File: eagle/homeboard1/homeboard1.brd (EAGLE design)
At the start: 100 x 80 mm, 17 parts, among them U1 XC3S400TQ144

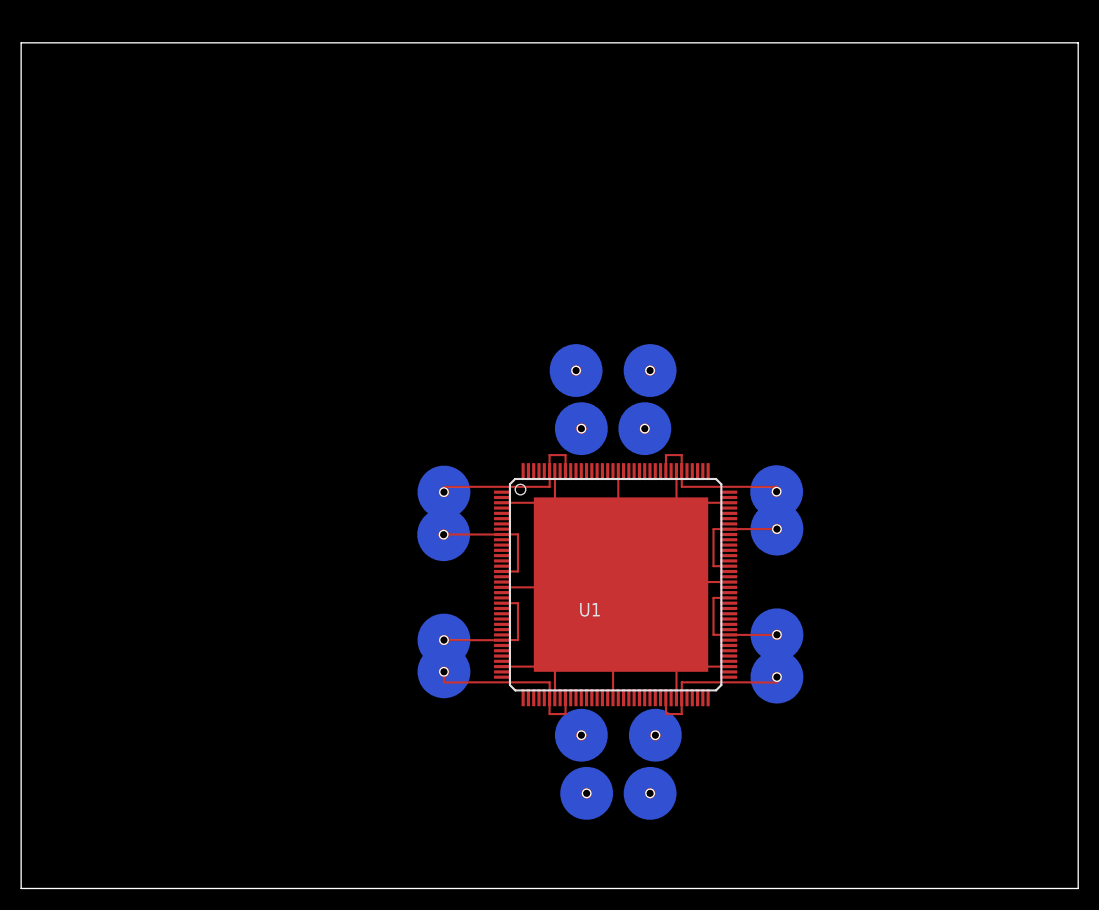
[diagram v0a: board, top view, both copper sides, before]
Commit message: added ram chip
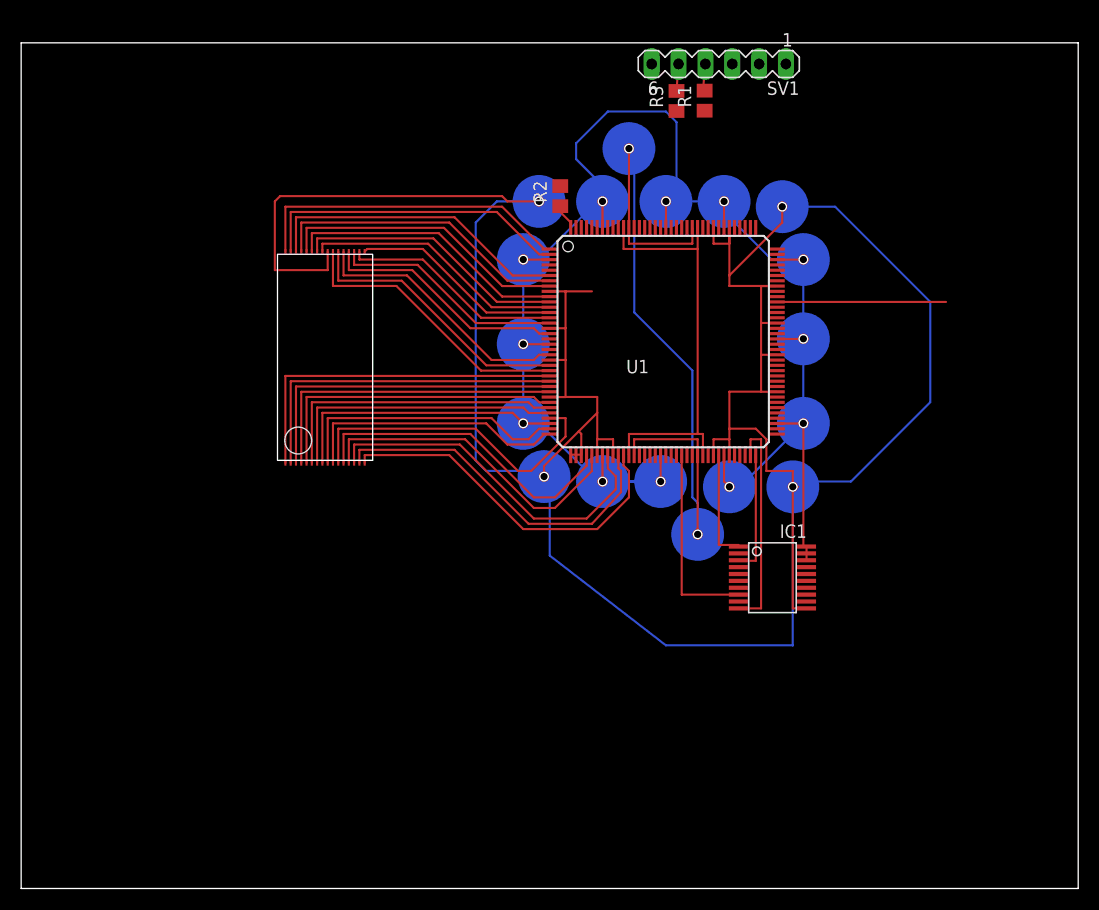
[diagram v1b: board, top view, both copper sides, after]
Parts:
- removed U$12, U$13, U$16, U$17, U$21, U$22, U$24, U$8, U$9: VIA_DIY, cpcfpga:VIA_DIY
- added IC1: XCF02S, smd-special:VO20
- added R1, R2, R3: 100, rcl:R0805
- added SV1: (no value), con-lstb:MA06-1
- added U$10, U$14, U$15, U$18, U$19, U$25, U$26, U$27, U$28, U$29, U$6, U$7: VIA_DIY, cpcfpga:VIA_DIY
- U$4: value VIA_DIY -> AS6C4008; device cpcfpga:VIA_DIY -> cpcfpga:TSOP32
- moved U$23 61.0 mm to (57.5, 70.0)
- moved U$3 51.7 mm to (49.0, 65.0)
- moved U$20 41.9 mm to (72.0, 64.5)
- moved U$4 30.8 mm to (28.8, 50.0), turned to 90 degrees
- moved U$1 26.7 mm to (64.0, 33.5)
- moved U1 23.4 mm to (60.7, 51.7)
- moved U$2 15.0 mm to (73.0, 38.0)
- moved U$5 11.0 mm to (49.5, 39.0)
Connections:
- removed net GND_B: U$12.B, U$13.B, U$16.B, U$17.B, U$20.B, U$5.B, U$8.B, U$9.B
- removed net VCCINT01: U$1.T, U1.P49
- new net N$10: U$4.P29, U1.P7
- new net N$11: U$4.P28, U1.P8
- new net N$14: U$14.T, U1.P34
- new net N$15: U$15.T, U1.P19
- new net N$22: U$4.P27, U1.P10
- new net N$23: U$4.P26, U1.P11
- new net N$24: U$4.P18, U1.P14
- new net N$25: U$25.T, U1.P54
- new net N$26: IC1.18, IC1.19, IC1.20, U$29.T, U1.P75
- new net N$27: U$4.P19, U1.P15
- new net N$28: U$28.T, U1.P91
- new net N$29: U$4.P20, U1.P17
- new net N$3: U$10.T, U1.P126
- new net N$30: U$4.P21, U1.P21
- new net N$31: U$4.P22, U1.P23
- new net N$32: U$4.P23, U1.P24
- new net N$33: U$4.P1, U1.P25
- new net N$34: U$4.P2, U1.P26
- new net N$35: U$4.P3, U1.P27
- new net N$36: U$4.P4, U1.P28
- new net N$37: U$4.P5, U1.P30
- new net N$38: U$4.P6, U1.P31
- new net N$39: U$4.P7, U1.P32
- new net N$40: U$4.P11, U1.P33
- new net N$41: U$4.P9, U1.P35
- new net N$42: U$4.P10, U1.P36
- new net N$43: U$4.P12, U1.P40
- new net N$44: U$4.P13, U1.P41
- new net N$45: U$4.P14, U1.P44
- new net N$46: U$4.P15, U1.P46
- new net N$47: U$4.P16, U1.P47
- new net N$5: U$4.P25, U1.P12
- new net N$6: U$4.P17, U1.P13
- new net N$7: U$4.P30, U1.P6
- new net TCK: IC1.6, R1.2, SV1.4
- new net TDI: IC1.4, SV1.3
- new net TDO: SV1.6, U1.P109
- new net TMS: IC1.5, R3.2, SV1.5
- net GND: now also IC1.11, U$2.B, U$20.B, U$3.B, U$3.T, U$4.P24, U$5.B, U$5.T, U1.P16, U1.P22, U1.P29, U1.P37, U1.P38, U1.P39, U1.P42, U1.P45, U1.P9; no longer U$20.T
- net N$1: now also U$4.P32, U1.P1; no longer U$5.T, U1.P16, U1.P9
- net N$12: now also R2.1, U1.P144; no longer U$16.T, U1.P101, U1.P94
- net N$13: now also IC1.17, R2.2; no longer U$17.T, U1.P114, U1.P117
- net N$16: now also R3.1, U1.P111; no longer U$22.T, U1.P48
- net N$17: now also IC1.7, U1.P143; no longer U$24.T, U1.P133
- net N$18: now also IC1.8, U1.P58; no longer U$23.T, U1.P61
- net N$19: now also IC1.3, U1.P72; no longer U$21.T, U1.P134
- net N$2: now also U$4.P31, U1.P2; no longer U$9.T, U1.P42, U1.P45
- net N$20: now also IC1.10, U1.P71; no longer U$21.B, U$22.B, U$3.B, U$4.B
- net N$21: now also U1.P98; no longer U$3.T, U1.P62
- net N$4: now also U$2.T, U$20.T, U1.P101, U1.P114, U1.P117, U1.P64, U1.P67, U1.P81, U1.P88, U1.P94; no longer U$8.T, U1.P22, U1.P29
- net N$8: now also R1.1, U1.P110; no longer U$12.T, U1.P64, U1.P67
- net N$9: now also IC1.1, U1.P65; no longer U$13.T, U1.P81, U1.P88
- net VCC: now also U$10.B, U$14.B, U$15.B, U$18.B, U$18.T, U$19.B, U$19.T, U$25.B, U$26.B, U$26.T, U$27.B, U$27.T, U$28.B, U$29.B, U$4.P8, U$6.B, U$6.T, U$7.B, U$7.T; no longer U1.P126, U1.P19, U1.P34, U1.P54, U1.P75, U1.P91
- net VCCAUX: now also U1.P134, U1.P48, U1.P62; no longer U$4.T
- net VCCINT23: now also U$23.T, U1.P133; no longer U$2.T
- net VCCINT_B: now also U$1.T, U1.P49, U1.P61; no longer U$2.B, U$24.B
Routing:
- net GND: track 16.6 -> 222.8 mm
- net VCCINT_B: track 0.00 -> 56.0 mm
- net N$4: track 12.0 -> 61.6 mm
- net VCCAUX: track 0.00 -> 39.4 mm
- net N$47: track 0.00 -> 34.1 mm
- net N$45: track 0.00 -> 34.1 mm
- net N$46: track 0.00 -> 33.8 mm
- net N$33: track 0.00 -> 33.3 mm
- net N$34: track 0.00 -> 32.3 mm
- net N$35: track 0.00 -> 31.3 mm
- net N$40: track 0.00 -> 31.0 mm
- net N$44: track 0.00 -> 30.9 mm
- net N$43: track 0.00 -> 30.5 mm
- net N$36: track 0.00 -> 30.3 mm
- net N$7: track 0.00 -> 29.6 mm
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
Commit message: improved ram chip layout
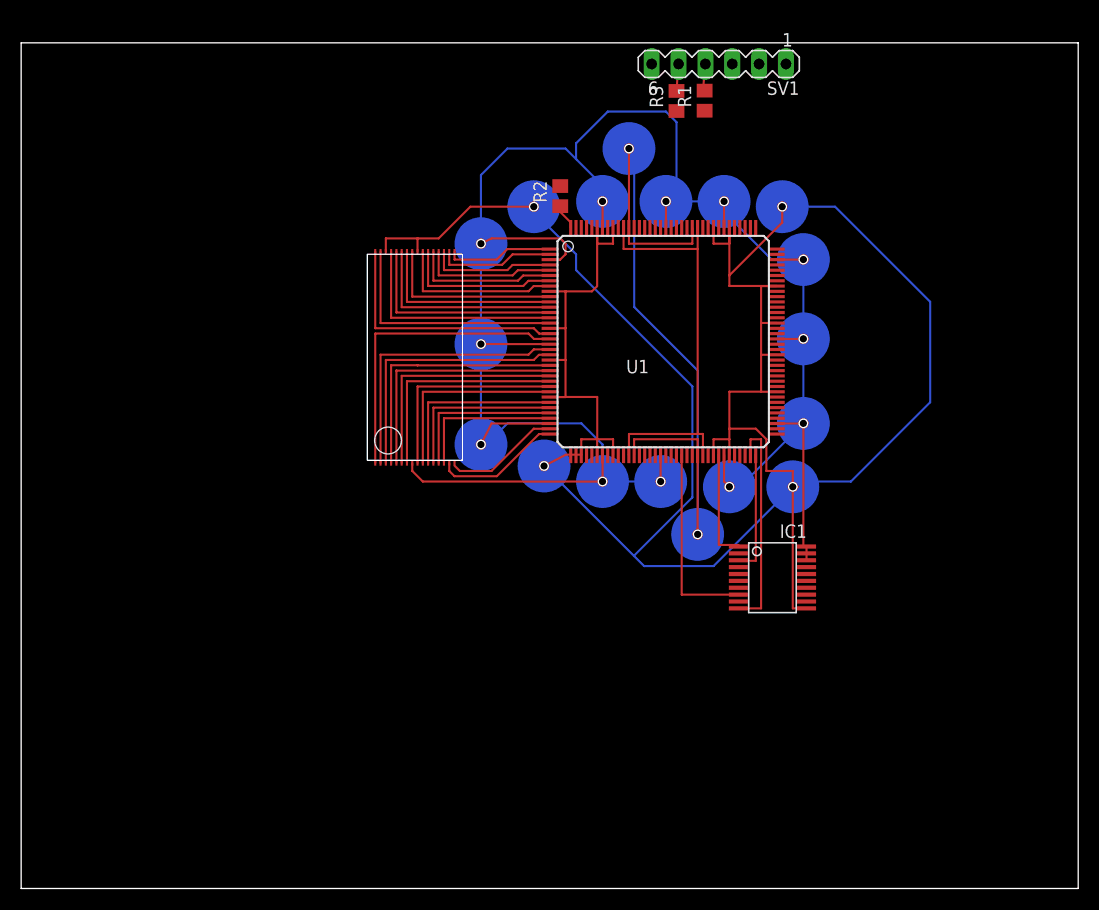
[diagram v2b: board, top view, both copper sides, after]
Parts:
- moved U$4 8.50 mm to (37.2, 50.0)
- moved U$14 4.47 mm to (43.5, 42.0)
- moved U$18 4.27 mm to (43.5, 61.0)
- moved U$15 4.00 mm to (43.5, 51.5)
- moved U$5 1.00 mm to (49.5, 40.0)
- moved U$3 0.71 mm to (48.5, 64.5)
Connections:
- removed net N$39: U$4.P7, U1.P32
- removed net N$40: U$4.P11, U1.P33
- removed net N$41: U$4.P9, U1.P35
- removed net N$42: U$4.P10, U1.P36
- new net N$48: U$4.P20, U1.P5
- new net N$49: U$4.P19, U1.P4
- new net N$50: U$4.P1, U1.P18
- new net N$52: U$4.P4, U1.P23
- new net N$53: U$4.P3, U1.P21
- new net N$54: U$4.P5, U1.P24
- new net N$55: U$4.P6, U1.P25
- new net N$56: U$4.P7, U1.P26
- net GND: now also U$4.P30
- net N$1: now also U$4.P17; no longer U$4.P32
- net N$10: now also U$4.P22; no longer U$4.P29
- net N$11: now also U$4.P23; no longer U$4.P28
- net N$2: now also U$4.P18; no longer U$4.P31
- net N$22: now also U$4.P25; no longer U$4.P27
- net N$24: now also U$4.P29; no longer U$4.P18
- net N$27: now also U$4.P31; no longer U$4.P19
- net N$29: now also U$4.P32; no longer U$4.P20
- net N$30: now also U$4.P10, U1.P28; no longer U$4.P21, U1.P21
- net N$31: now also U$4.P11, U1.P30; no longer U$4.P22, U1.P23
- net N$32: now also U$4.P12, U1.P31; no longer U$4.P23, U1.P24
- net N$33: now also U$4.P2, U1.P20; no longer U$4.P1, U1.P25
- net N$34: now also U$4.P13, U1.P32; no longer U$4.P2, U1.P26
- net N$35: now also U$4.P14, U1.P33; no longer U$4.P3, U1.P27
- net N$36: now also U$4.P9, U1.P27; no longer U$4.P4, U1.P28
- net N$37: now also U$4.P16, U1.P35; no longer U$4.P5, U1.P30
- net N$38: now also U$4.P15, U1.P36; no longer U$4.P6, U1.P31
- net N$43: no longer U$4.P12
- net N$44: no longer U$4.P13
- net N$45: no longer U$4.P14
- net N$46: no longer U$4.P15
- net N$47: no longer U$4.P16
- net N$5: now also U$4.P27; no longer U$4.P25
- net N$6: now also U$4.P28; no longer U$4.P17
- net N$7: now also U$4.P21; no longer U$4.P30
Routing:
- net N$47: track 34.1 -> 0.00 mm
- net N$45: track 34.1 -> 0.00 mm
- net N$46: track 33.8 -> 0.00 mm
- net N$40: track 31.0 -> 0.00 mm
- net N$44: track 30.9 -> 0.00 mm
- net N$43: track 30.5 -> 0.00 mm
- net GND: track 222.8 -> 193.7 mm
- net N$50: track 0.00 -> 29.0 mm
- net N$39: track 27.5 -> 0.00 mm
- net N$41: track 26.5 -> 0.00 mm
- net N$42: track 25.5 -> 0.00 mm
- net N$53: track 0.00 -> 25.5 mm
- net N$52: track 0.00 -> 24.3 mm
- net N$54: track 0.00 -> 23.3 mm
- net N$55: track 0.00 -> 22.3 mm
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
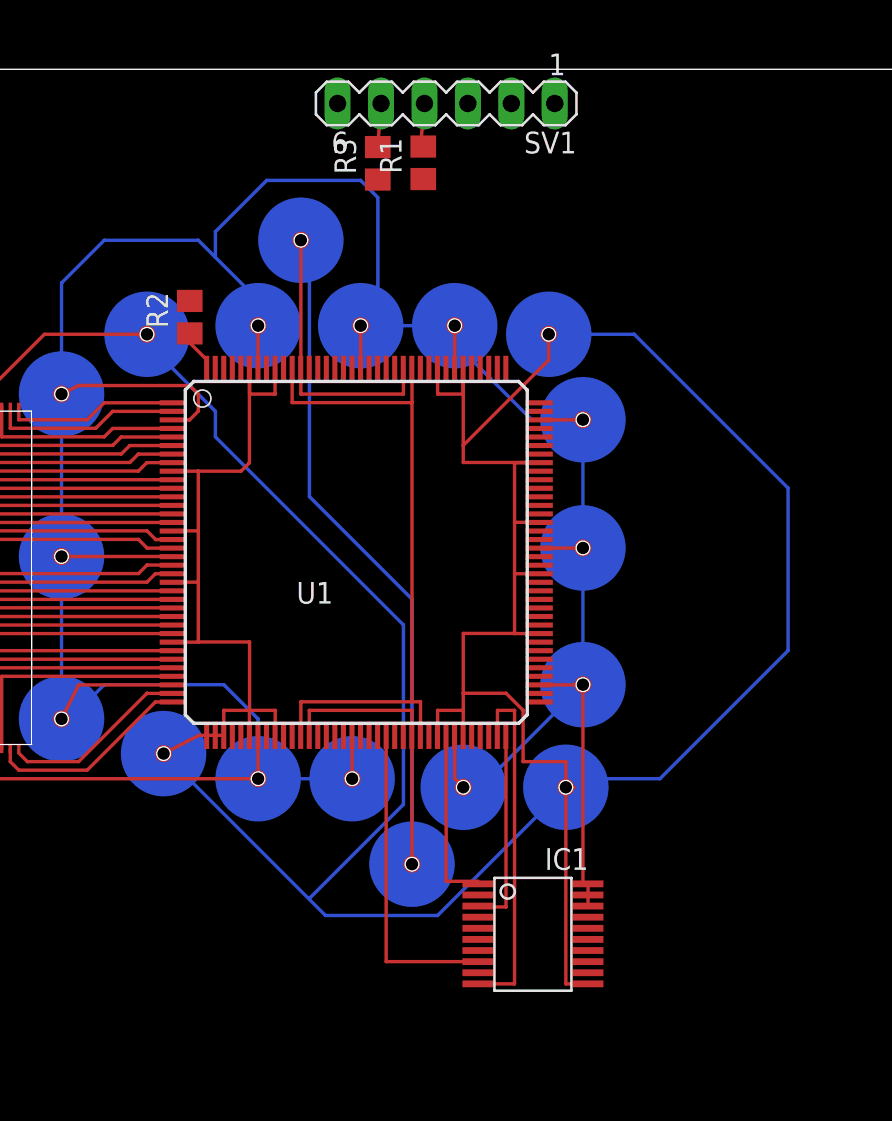
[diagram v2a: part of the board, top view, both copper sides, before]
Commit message: try from scratch with no dru errors
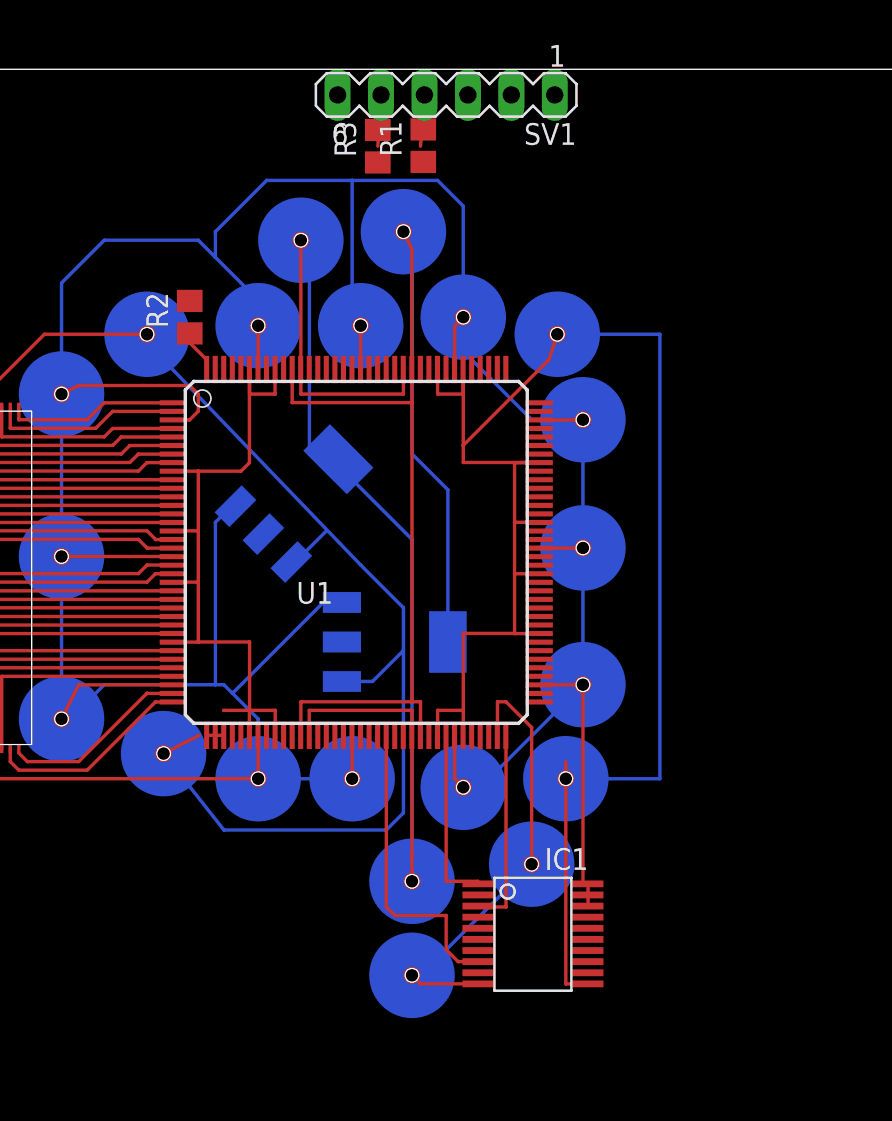
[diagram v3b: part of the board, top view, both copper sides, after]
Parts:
- added U$11, U$12, U$13: VIA_DIY, cpcfpga:VIA_DIY
- added U$8: 2.5V, cpcfpga:SOT223
- added U$9: 1.2V, cpcfpga:SOT223
- SV1: value (none) -> jtag
- moved R1 1.00 mm to (64.7, 75.5)
- moved R3 1.00 mm to (62.0, 75.5)
- moved U$1 1.00 mm to (64.0, 32.5)
- moved U$7 0.71 mm to (67.0, 65.5)
- moved SV1 0.50 mm to (66.0, 78.5)
- moved U$2 0.50 mm to (73.0, 38.5)
- moved U$20 0.50 mm to (72.5, 64.5)
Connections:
- removed net N$21: U1.P98
- removed net N$43: U1.P40
- removed net N$44: U1.P41
- removed net N$45: U1.P44
- removed net N$46: U1.P46
- removed net N$47: U1.P47
- removed net VCCINT23: U$23.T, U1.P121, U1.P133
- new net N$39: U$11.B, U$8.4
- new net N$40: IC1.10, U$12.T
- new net N$41: U$12.B, U$13.B
- net GND: now also U$8.1, U$9.1
- net N$20: now also U$13.T; no longer IC1.10
- net VCC: now also U$8.3, U$9.3
- net VCCAUX: now also U$11.T
- net VCCINT_B: now also U$23.T, U$9.4, U1.P121, U1.P133
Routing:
- net VCC: track 170.0 -> 195.8 mm
- net N$39: track 0.00 -> 25.0 mm
- net GND: track 193.7 -> 172.1 mm
- net VCCINT_B: track 56.0 -> 75.0 mm
- net VCCINT23: track 16.5 -> 0.00 mm
- net N$4: track 61.6 -> 51.7 mm
- net N$41: track 0.00 -> 9.69 mm
- net VCCAUX: track 39.4 -> 47.5 mm
- net N$20: track 20.7 -> 12.6 mm
- net N$40: track 0.00 -> 4.06 mm
- net N$18: track 18.6 -> 17.8 mm
